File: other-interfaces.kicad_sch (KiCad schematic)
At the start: 24 parts, among them J8 DM3AT-SF-PEJM5, J9 BM04B-SRSS-TB-LF-SN

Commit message: Introduce component standardization
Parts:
- C117, C120: renamed from C?; value (none) -> C_100n_0402; footprint (none) -> sa800u-baseboard-hw-footprints:C_0402_1005Metric; Author (none) -> Antmicro; Dielectric (none) -> X5R; License (none) -> Apache-2.0; Voltage (none) -> 50V
- C118: footprint sa800u-baseboard-hw-footprints:0402-cap -> sa800u-baseboard-hw-footprints:C_0402_1005Metric; Author (none) -> Antmicro; Dielectric (none) -> C0G; License (none) -> Apache-2.0; MPN MC0402N100D500CT -> GCM1555C1H100GA16D; Manufacturer MULTICOMP -> Murata; Voltage (none) -> 50V
- C119: footprint sa800u-baseboard-hw-footprints:0603-cap -> sa800u-baseboard-hw-footprints:C_0603_1608Metric; Author (none) -> Antmicro; License (none) -> Apache-2.0
- D22, D23: renamed from D?; value (none) -> PUSB3F96X_PASS; footprint (none) -> sa800u-baseboard-hw-footprints:Nexperia_DFN-10_2.5x1mm_P0.5mm; Author (none) -> Antmicro; License (none) -> Apache-2.0
- J8: Author (none) -> Antmicro; License (none) -> Apache-2.0; Manufacturer HIROSE -> Hirose
- J9: Author (none) -> Antmicro; License (none) -> Apache-2.0
- R100, R101, R102, R96, R97, R98: footprint sa800u-baseboard-hw-footprints:0402-res -> sa800u-baseboard-hw-footprints:R_0402_1005Metric; Author (none) -> Antmicro; License (none) -> Apache-2.0; MPN CRCW040233R0FKED -> CR0402-FX-33R0GLF; Manufacturer Vishay -> Bourns; Tolerance (none) -> 1%
- R103, R104: renamed from R?; value (none) -> R_2k_0402; footprint (none) -> sa800u-baseboard-hw-footprints:R_0402_1005Metric; Author (none) -> Antmicro; License (none) -> Apache-2.0; MPN CRCW04022K00FKED -> CR0402-FX-2001GLF; Manufacturer VISHAY -> Bourns; Tolerance (none) -> 1%
- R94: footprint sa800u-baseboard-hw-footprints:0402-res -> sa800u-baseboard-hw-footprints:R_0402_1005Metric; Author (none) -> Antmicro; License (none) -> Apache-2.0; MPN CRCW0402100KFKEDHP -> CR0402-FX-1003GLF; Manufacturer VISHAY -> Bourns; Tolerance (none) -> 1%
- R95: footprint sa800u-baseboard-hw-footprints:0402-res -> sa800u-baseboard-hw-footprints:R_0402_1005Metric; Author (none) -> Antmicro; License (none) -> Apache-2.0; Manufacturer BOURNS -> Bourns; Tolerance (none) -> 1%
- R99: footprint sa800u-baseboard-hw-footprints:0402-res -> sa800u-baseboard-hw-footprints:R_0402_1005Metric; Author (none) -> Antmicro; Current (none) -> 1A; License (none) -> Apache-2.0; Manufacturer PANASONIC -> Panasonic
- TP44, TP45, TP46, TP47: renamed from TP?; value (none) -> TP_0.75mm_SMD; footprint (none) -> sa800u-baseboard-hw-footprints:TP_SMD_0.75mm; symbol sa800u-baseboard-hw:TP_SMD_0_75MM -> sa800u-baseboard-hw:TP_0.75mm_SMD; Author (none) -> Antmicro; License (none) -> Apache-2.0
- U16: renamed from U?; value (none) -> NTS0102_XSON; footprint (none) -> sa800u-baseboard-hw-footprints:XSON-8_1x1.95mm_P0.5mm; symbol sa800u-baseboard-hw:NTS0102GT -> sa800u-baseboard-hw:NTS0102_XSON; Author (none) -> Antmicro; License (none) -> Apache-2.0; Manufacturer NXP Semiconductors -> NXP
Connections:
- no-connect marks 0 -> 1
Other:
- moved on the sheet: C117, C118, C119, C120, R100, R101, R102, R103, R104, R94, R95, R96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

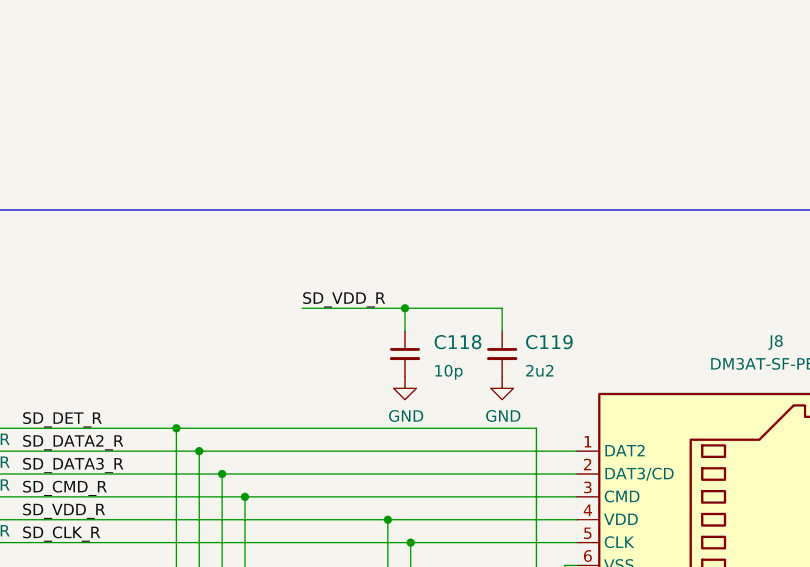
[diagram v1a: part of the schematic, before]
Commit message: Add OHP assets
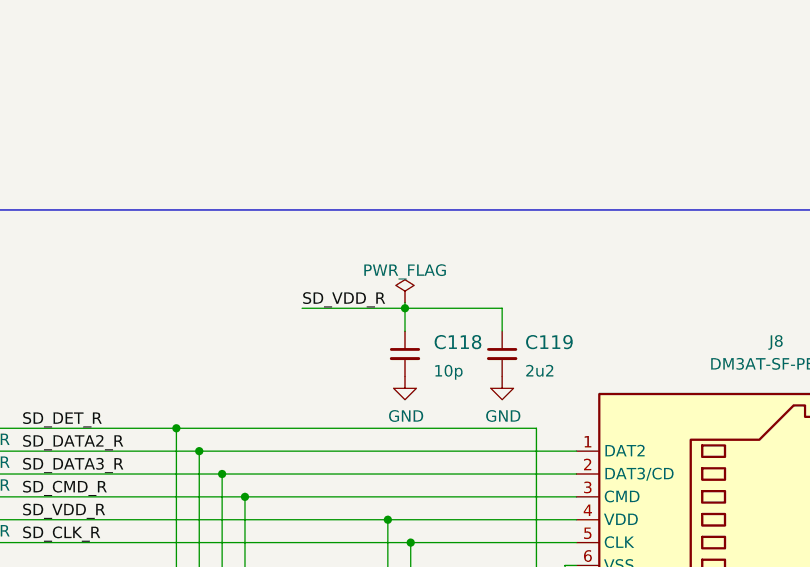
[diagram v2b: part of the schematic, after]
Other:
- company: (none) -> Antmicro Ltd.
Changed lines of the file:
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@@
   (title_block
     (title "SA800U (Snapdragon 845) Baseboard")
-    (date "2023-07-27")
-    (rev "1.0.2")
+    (date "2023-10-19")
+    (rev "1.0.3")
+    (company "Antmicro Ltd.")
     (comment 1 "www.antmicro.com")
-    (comment 2 "Antmicro Ltd.")
   )
   (junction (at 131.699 70.866) (diameter 0) (color 0 0 0 0)
@@
     (stroke (width 0) (type default) (color 0 0 0 0))
   )
+  (wire (pts (xy 154.559 54.356) (xy 154.559 54.991))
+    (stroke (width 0) (type default) (color 0 0 0 0))
+  )
   (wire (pts (xy 87.249 58.166) (xy 92.329 58.166))
     (stroke (width 0) (type default) (color 0 0 0 0))
@@
     )
     (pin "1")
+  )
+  (symbol (lib_id "sa800u-baseboard-hw:PWR_FLAG") (at 154.559 54.356 0) (unit 1)
+    (in_bom yes) (on_board yes)
+    (property "Reference" "#FLG0107" (id 0) (at 154.559 52.451 0)
+      (effects (font (size 1.27 1.27)) hide)
+    )
+    (property "Value" "PWR_FLAG" (id 1) (at 154.559 50.8 0))
+    (property "Footprint" "" (id 2) (at 154.559 54.356 0)
+      (effects (font (size 1.27 1.27)) hide)
+    )
+    (property "Datasheet" "~" (id 3) (at 154.559 54.356 0)
+      (effects (font (size 1.27 1.27)) hide)
+    )
+    (pin "1")
